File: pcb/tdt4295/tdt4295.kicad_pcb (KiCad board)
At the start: 6 copper layers, 183 parts, among them J101 ARM 20 Pin Debug Header, J102 MCU USART1 Header, J103 DM1AA-SF-PEJ(21), J104 MCU GPIO Header, J301 FPGA__debug, J501 618015330923, J502 FPGA GPIO, P201 690-005-299-043, U101 EFM32GG12B810F1024GQ64, U102 COM-09032 Joystick, U103 COM-09032 Joystick, U201 PHDMI2AB4, U202 TPS54294, U203 TPS54294, U301 S25FL127SABMFV101, U302 NUP4114UCW1T2G, U303 XC7A100T-FTG256-tdt4295, U501 NUP4114UCW1T2G, U502 NUP4114UCW1T2G, U503 NUP4114UCW1T2G, U504 NUP4114UCW1T2G, U601 DSC1001AL5-100.0000, Y101 48MHz

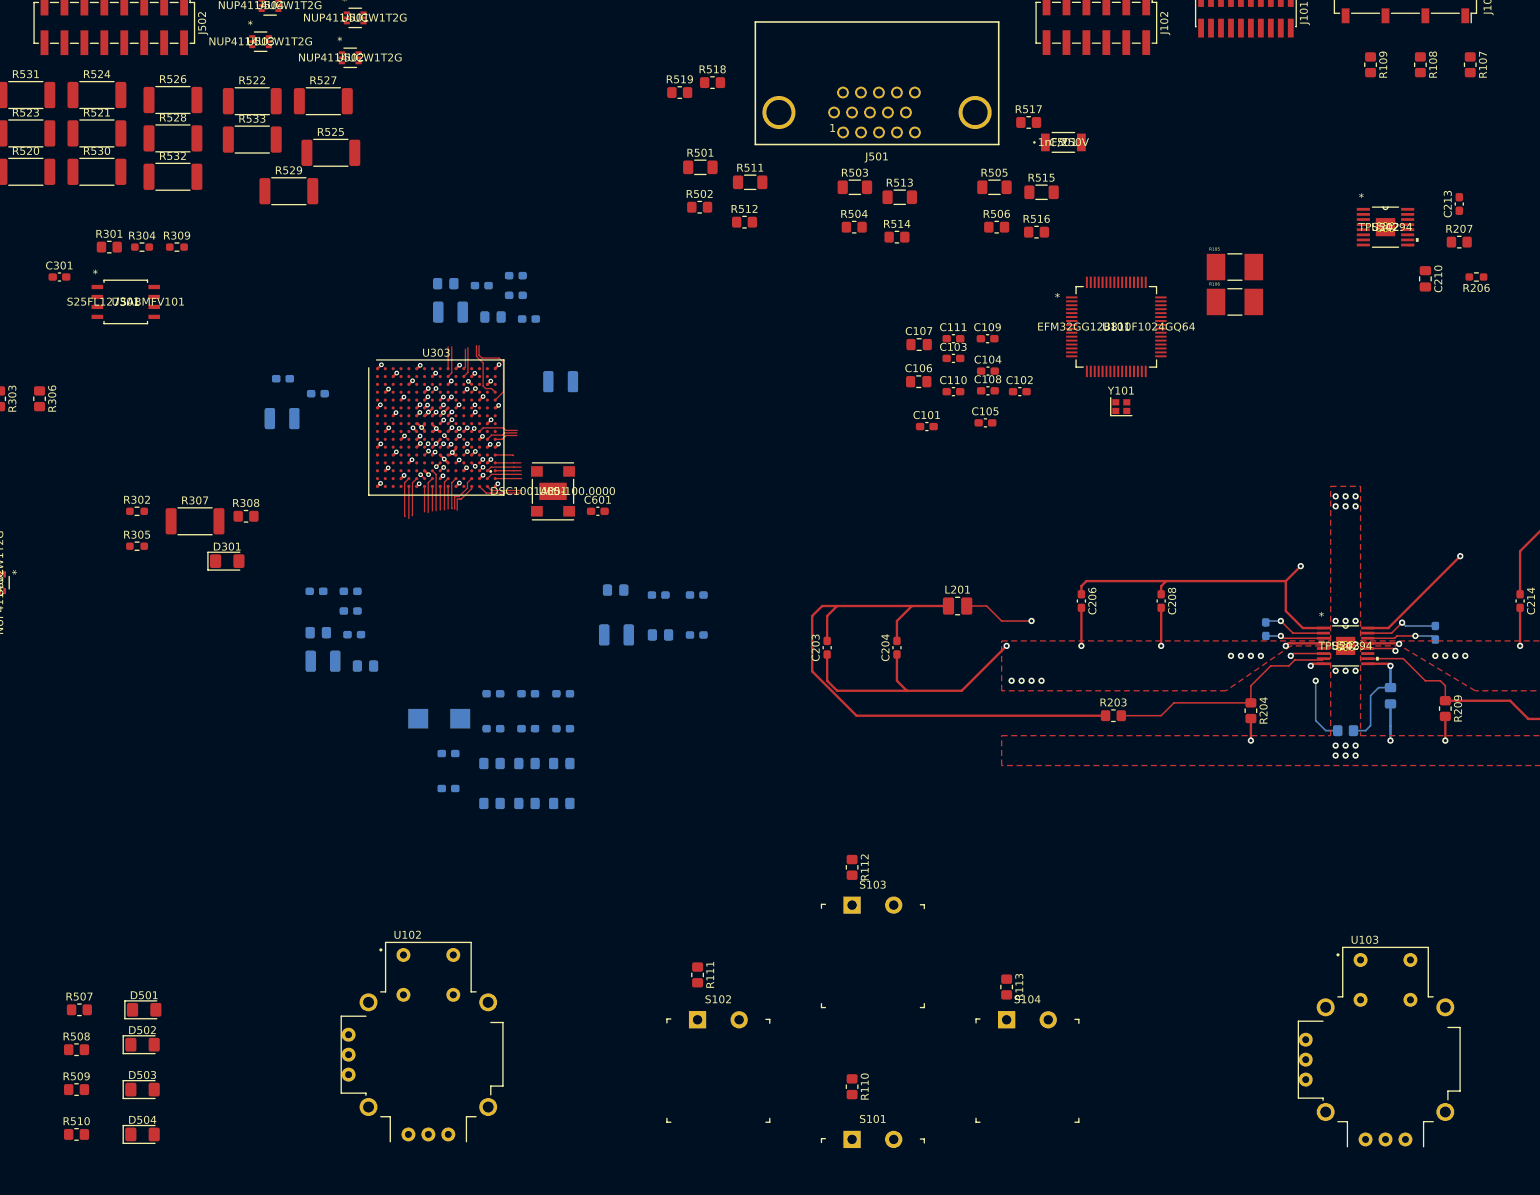
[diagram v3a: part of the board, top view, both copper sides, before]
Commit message: correct 330 Ohm footprints, route some more FPGA
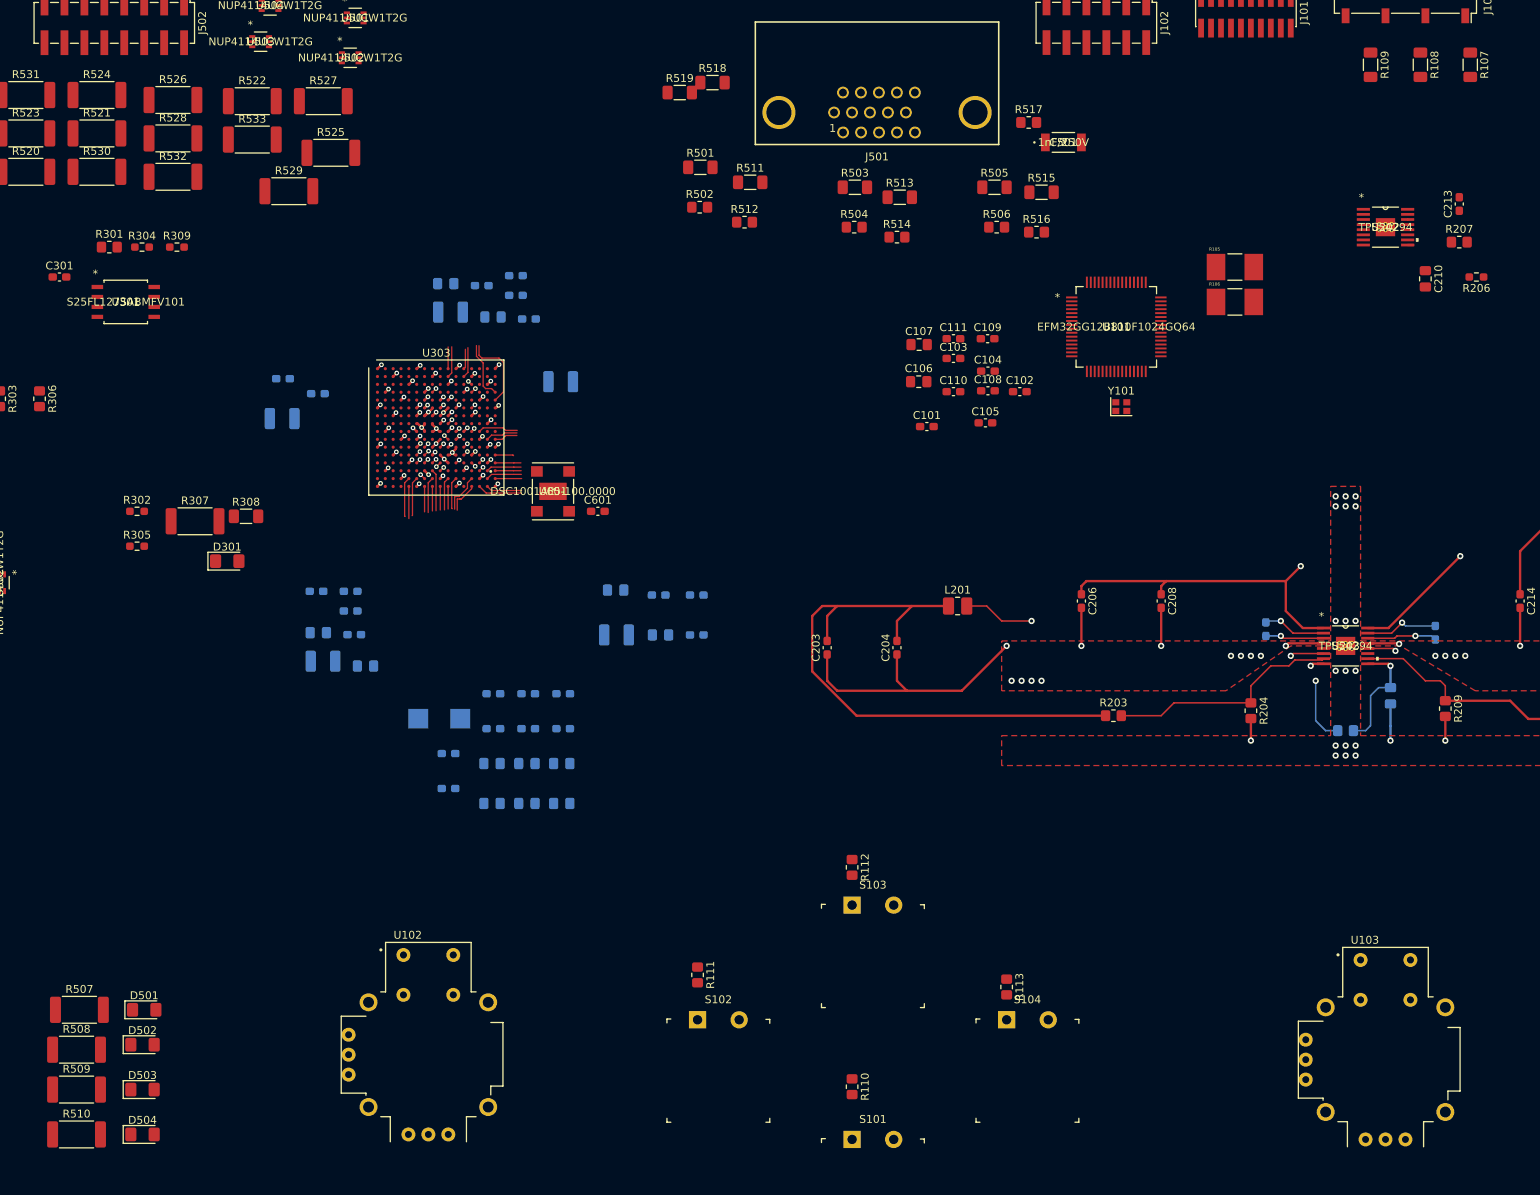
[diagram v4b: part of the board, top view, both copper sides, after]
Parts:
- R107, R108, R109, R308, R518, R519: footprint Resistor_SMD:R_0805_2012Metric_Pad1.20x1.40mm_HandSolder -> Resistor_SMD:R_1206_3216Metric_Pad1.30x1.75mm_HandSolder
- R507, R508, R509, R510: footprint Resistor_SMD:R_0805_2012Metric_Pad1.20x1.40mm_HandSolder -> Resistor_SMD:R_2512_6332Metric_Pad1.40x3.35mm_HandSolder
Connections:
- net FPGA_EXT_IO30 renamed Net-(U303-PadK12)
- U302 pad 5: (no net) -> +3V3
- U302 pad 6: +3V3 -> /FPGA/TMS_JTAG
- U501 pad 5: (no net) -> +3V3
- U501 pad 6: +3V3 -> Net-(J502-Pad11)
- U502 pad 5: (no net) -> +3V3
- U502 pad 6: +3V3 -> Net-(J502-Pad3)
- U503 pad 5: (no net) -> +3V3
- U503 pad 6: +3V3 -> Net-(J502-Pad4)
- U504 pad 5: (no net) -> +3V3
- U504 pad 6: +3V3 -> Net-(J502-Pad12)
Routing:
- net FPGA_DONE: track 0.69 -> 14.4 mm
- net /FPGA/TMS_JTAG: track 11.5 -> 0.72 mm
- net VGA_B2: track 0.00 -> 9.99 mm, vias 0 -> 1
- net /FPGA/TCK_JTAG: track 11.3 -> 1.39 mm
- net VGA_B3: track 0.00 -> 7.95 mm, vias 0 -> 1
- net /FPGA/TDO_JTAG: track 0.00 -> 0.68 mm, vias 0 -> 1
- net /FPGA/TDI_JTAG: track 0.00 -> 0.62 mm, vias 0 -> 1

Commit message: more FPGA routing
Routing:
- net /FPGA/TCK_JTAG: track 1.39 -> 16.2 mm
- net /FPGA/TDO_JTAG: track 0.68 -> 11.4 mm
- net /FPGA/TMS_JTAG: track 0.72 -> 10.0 mm
- net /FPGA/TDI_JTAG: track 0.62 -> 9.42 mm, vias 1 -> 0
- net +3V3: track 105.1 -> 104.5 mm, vias 14 -> 13

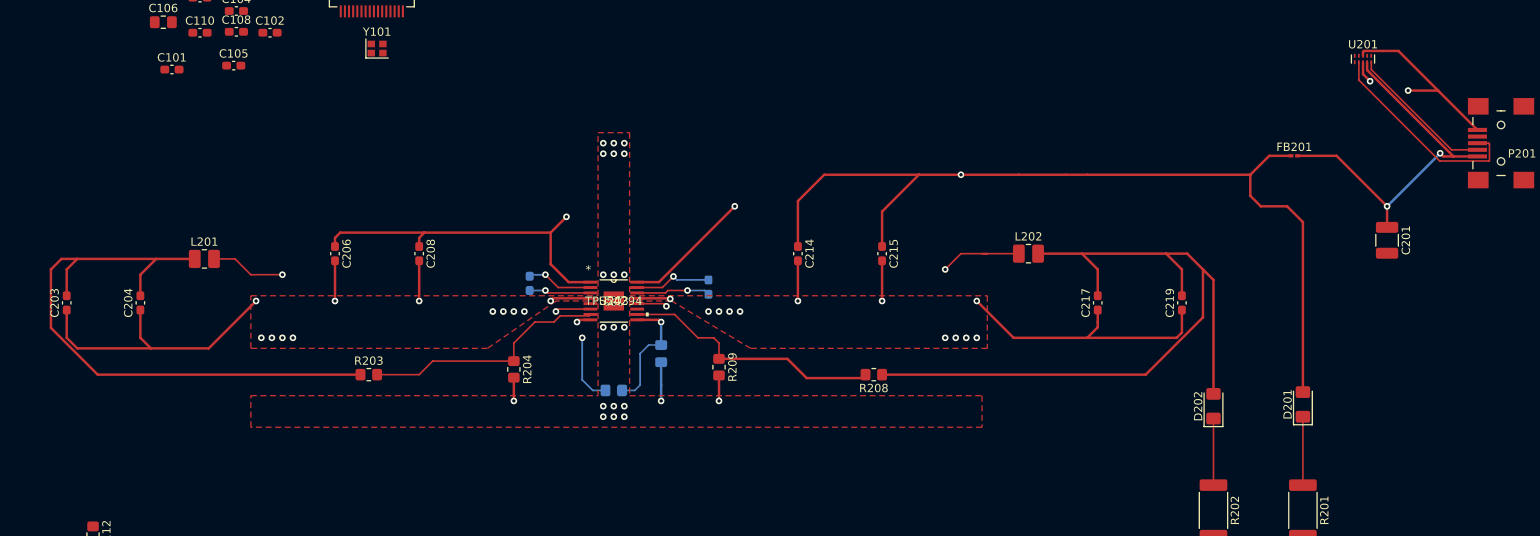
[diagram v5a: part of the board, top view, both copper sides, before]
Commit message: track width rules
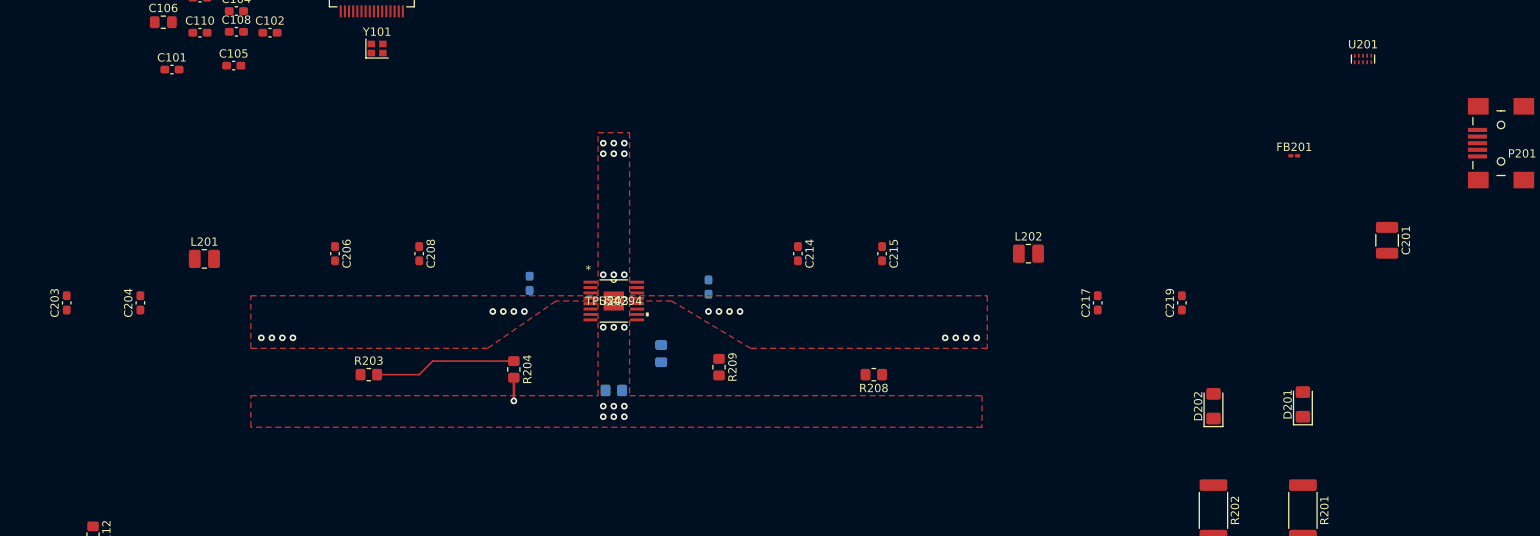
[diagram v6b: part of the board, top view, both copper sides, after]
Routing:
- net +5V: track 182.5 -> 1.80 mm, vias 3 -> 0
- net GND: track 193.8 -> 42.4 mm, vias 88 -> 75
- net +3V3: track 104.5 -> 9.10 mm
- net +1V8: track 78.1 -> 3.20 mm
- net Net-(C212-Pad2): track 51.4 -> 0.00 mm, vias 2 -> 0
- net Net-(C209-Pad2): track 49.0 -> 0.00 mm, vias 2 -> 0
- net Net-(C201-Pad1): track 45.3 -> 0.00 mm, vias 2 -> 0
- net Net-(R205-Pad2): track 32.6 -> 0.00 mm, vias 3 -> 0
- net Net-(R208-Pad2): track 32.0 -> 0.00 mm
- net USB_D+: track 25.5 -> 0.00 mm
- net USB_D-: track 17.7 -> 0.00 mm
- net Net-(C211-Pad1): track 15.0 -> 0.00 mm, vias 1 -> 0
- net Net-(R203-Pad2): track 30.0 -> 17.2 mm
- net Net-(C212-Pad1): track 9.34 -> 0.00 mm, vias 1 -> 0
- net Net-(D201-Pad1): track 8.25 -> 0.00 mm
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- removed copper zone on +PWR, net +5V

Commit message: significantly sexier power regulation
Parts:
- C210, C213: moved to B.Cu
- moved C203 54.8 mm to (193.7, 107.5)
- moved C204 51.1 mm to (198.8, 107.5)
- moved L201 48.7 mm to (203.9, 102.9)
- moved D201 43.2 mm to (332.1, 109.0)
- moved D202 43.2 mm to (321.3, 109.2)
- moved R201 43.2 mm to (332.1, 121.8)
- moved R202 43.2 mm to (321.3, 121.8)
- moved R203 38.7 mm to (214.3, 113.7)
- moved C206 38.4 mm to (209.6, 100.3)
- moved C208 33.4 mm to (214.6, 100.3)
- moved C209 26.2 mm to (221.0, 102.2)
- moved C211 24.8 mm to (234.9, 112.0)
- moved U203 24.5 mm to (229.2, 104.8)
- moved R204 24.2 mm to (217.8, 108.0), turned to 180 degrees
- moved R205 23.9 mm to (229.2, 113.0)
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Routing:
- net +3V3: track 9.10 -> 100.7 mm
- net +1V8: track 3.20 -> 94.9 mm
- net Net-(R205-Pad2): track 0.00 -> 42.4 mm, vias 0 -> 3
- net +5V: track 1.80 -> 36.9 mm
- net GND: track 42.4 -> 68.5 mm
- net Net-(C212-Pad2): track 0.00 -> 23.7 mm, vias 0 -> 2
- net Net-(C209-Pad2): track 0.00 -> 23.7 mm, vias 0 -> 2
- net Net-(R208-Pad2): track 0.00 -> 18.1 mm
- net Net-(C211-Pad1): track 0.00 -> 12.6 mm, vias 0 -> 1
- net R1_PG: track 0.00 -> 6.73 mm, vias 0 -> 1
- net Net-(C212-Pad1): track 0.00 -> 6.17 mm, vias 0 -> 1
- net Net-(C209-Pad1): track 0.00 -> 6.17 mm, vias 0 -> 1
- net Net-(R203-Pad2): track 17.2 -> 19.3 mm
- added copper zone on F.Cu, net +5V
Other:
- net class Default: trace_width 0.2 -> 0.3
- net class HS Bus added: clearance 0.2, trace_width 0.2, via_dia 0.8, via_drill 0.4
- net class Power: trace_width 0.3 -> 0.6
- net class Power narrow added: clearance 0.2, trace_width 0.4, via_dia 0.8, via_drill 0.4

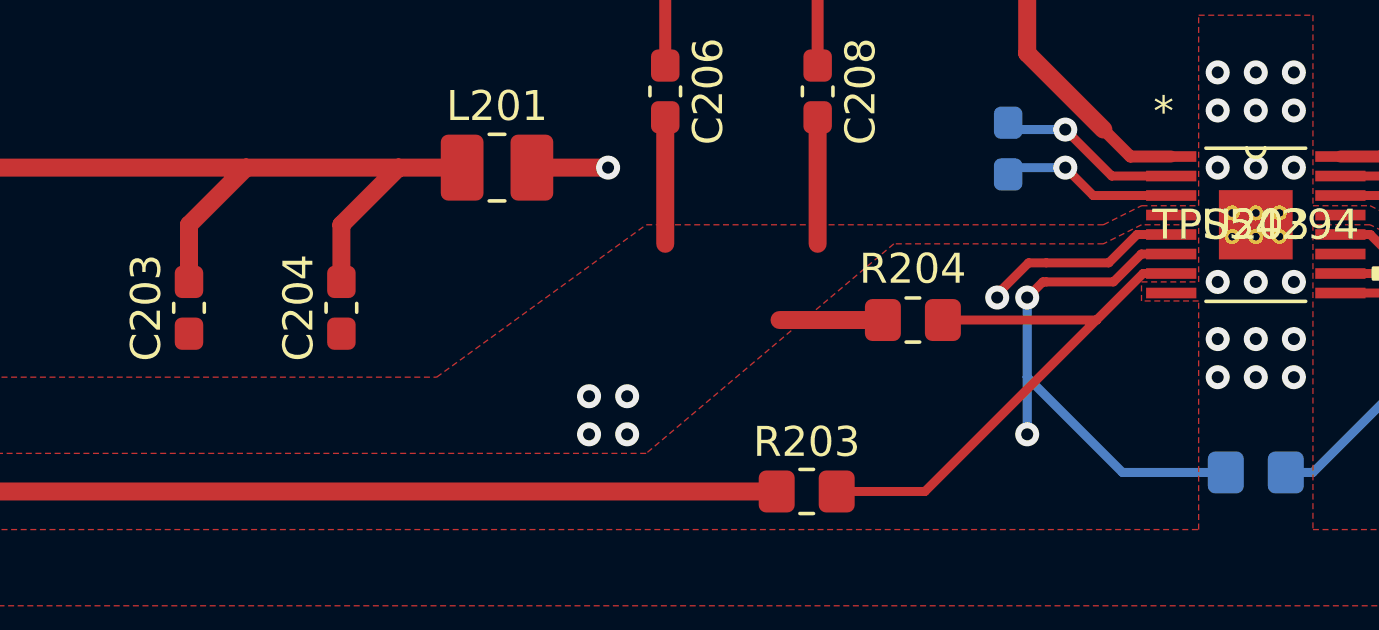
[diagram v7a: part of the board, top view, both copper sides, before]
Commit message: fix clearance & unconnected regulator caps
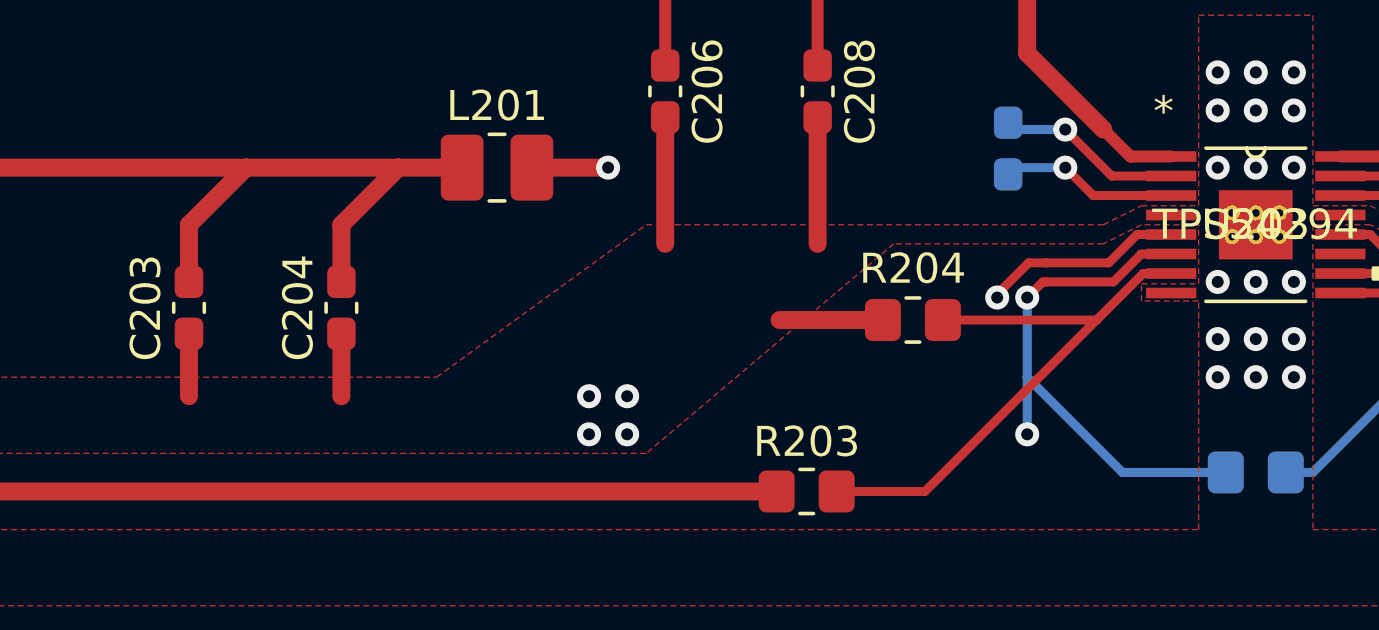
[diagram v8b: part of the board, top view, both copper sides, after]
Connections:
- U203 pad V: (no net) -> GND
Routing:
- net GND: track 68.5 -> 72.7 mm
